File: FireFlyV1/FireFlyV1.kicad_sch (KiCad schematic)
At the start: 76 parts, among them J1 Conn_01x03, J2 Conn_01x03, J3 Conn_01x03, J4 Conn_01x03, J5 Conn_01x03, SW1 TS-1187A-B-A-B, SW2 TS-1187A-B-A-B, U1 RP2040, U2 W25Q32JVSS, U3 AMS1117-3.3, U5 MCP6001T-I/OT, U6 74HC595D,118, U7 PEC12R-4215F-S0024, X1 X322512MSB4SI

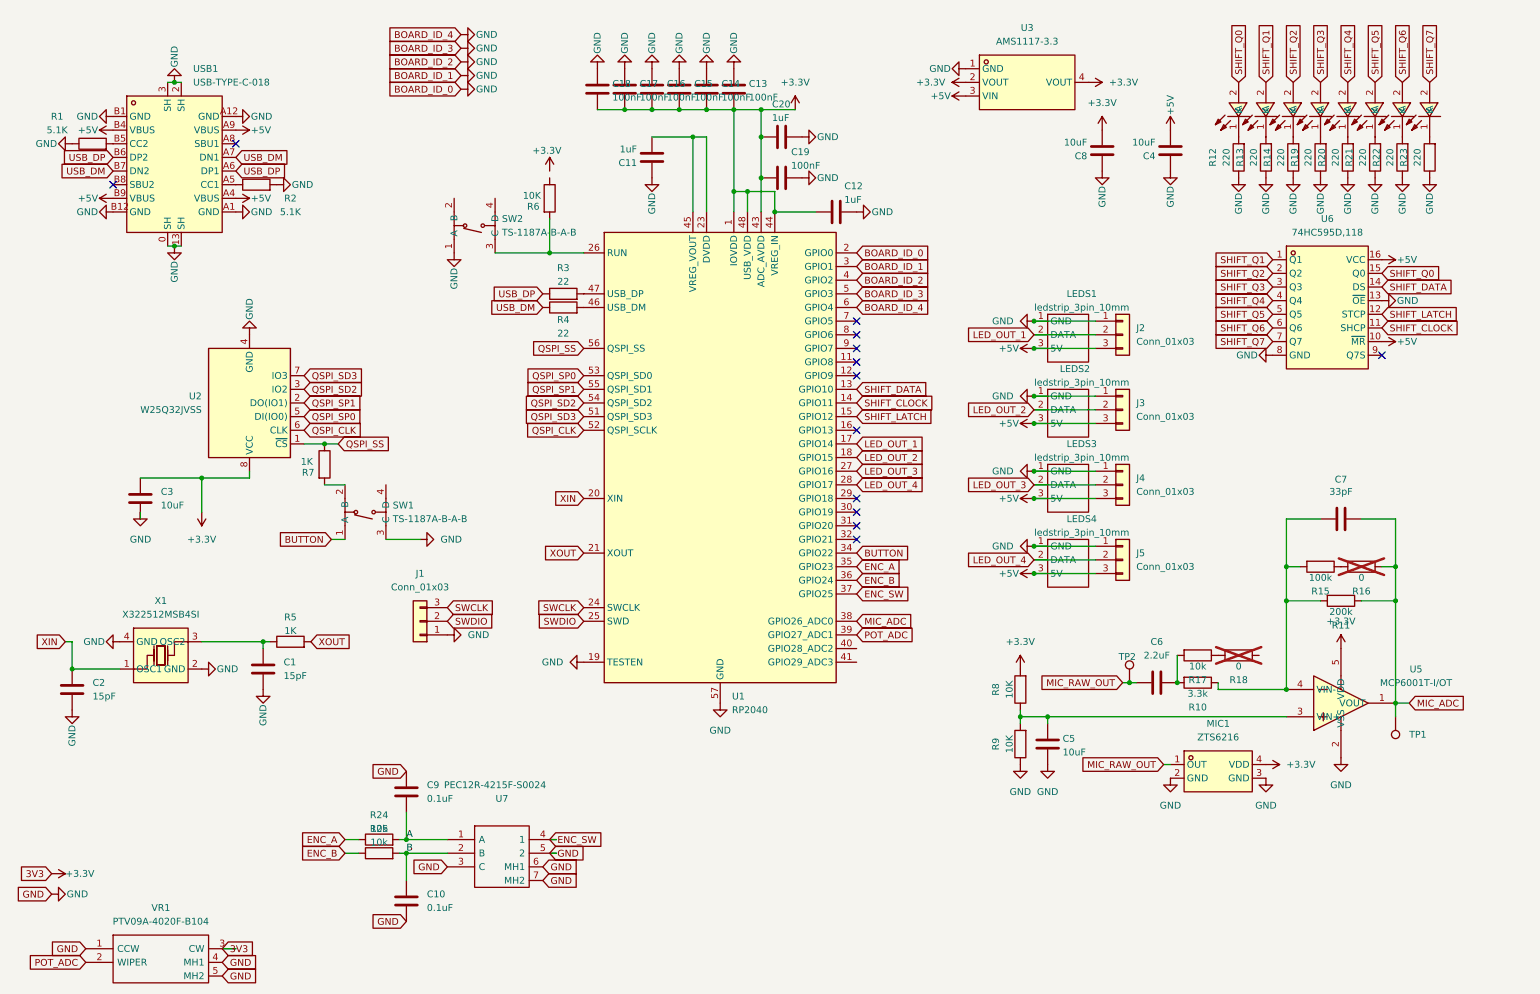
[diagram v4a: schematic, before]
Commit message: FireFlyV1 components layout initial thoughts
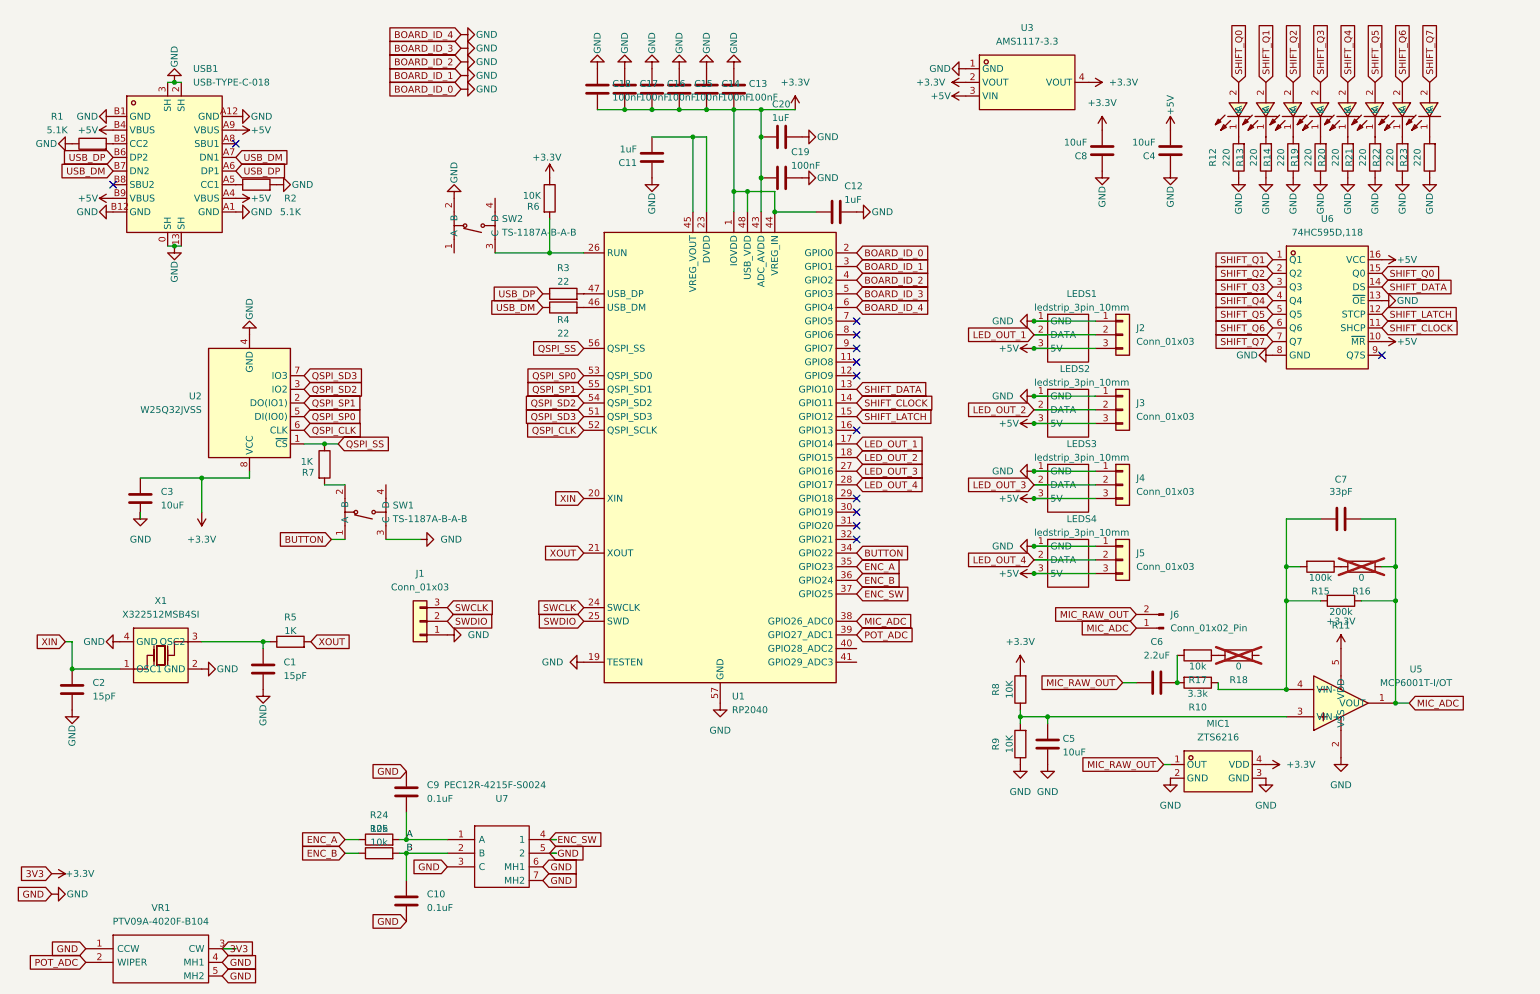
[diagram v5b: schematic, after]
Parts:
- removed TP1, TP2: TestPoint, TestPoint:TestPoint_Loop_D1.80mm_Drill1.0mm_Beaded, symbol Connector:TestPoint
- added J6: Conn_01x02_Pin, Connector_PinHeader_2.54mm:PinHeader_1x02_P2.54mm_Vertical, symbol Connector:Conn_01x02_Pin
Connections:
- net +3.3V: now also R6.1
- net GND: now also SW2.2 (B); no longer SW2.1 (A)
- net MIC_ADC: now also J6.1 (Pin_1)
- net MIC_RAW_OUT: now also J6.2 (Pin_2)

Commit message: FireFlyV1 mostly fit on the board
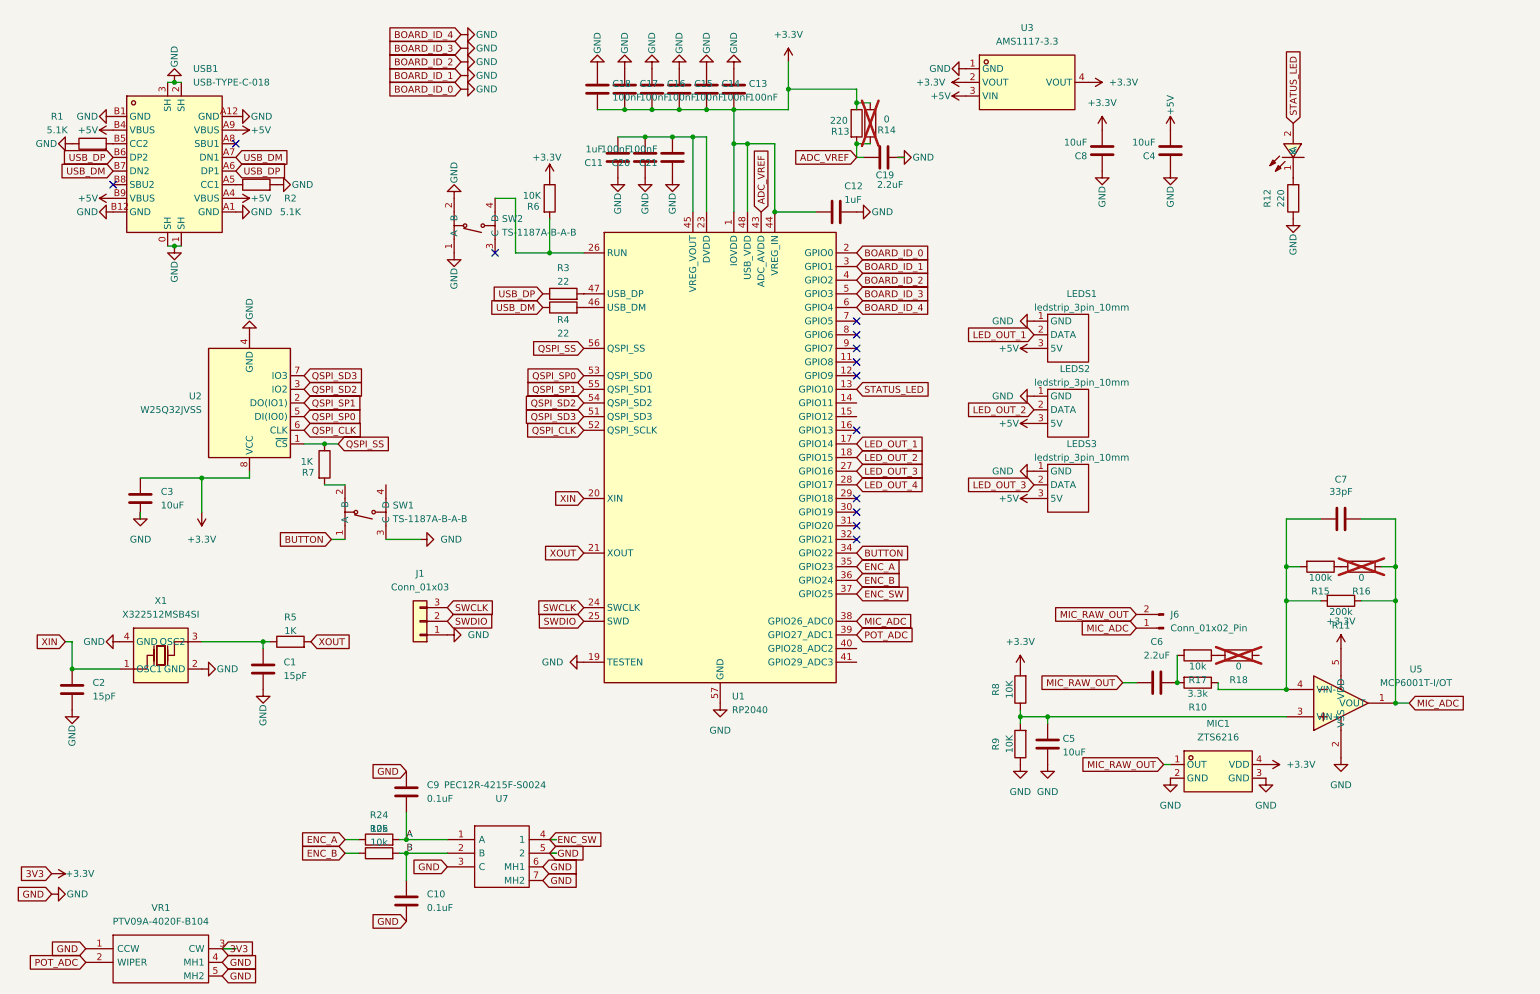
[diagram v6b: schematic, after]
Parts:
- removed J2, J3, J4, J5: Conn_01x03, Connector_PinHeader_2.54mm:PinHeader_1x03_P2.54mm_Vertical, symbol Connector_Generic:Conn_01x03
- removed LED2, LED3, LED4, LED5, LED6, LED7, LED8: KT-0603R, easyeda2kicad:LED0603-RD, symbol easyeda2kicad:KT-0603R
- removed LEDS4: ledstrip_3pin_10mm, mouser:ledstrip_3pin_10mm, symbol kylarLEDs:ledstrip_3pin_10mm
- removed R19, R20, R21, R22, R23: 220, Resistor_SMD:R_0402_1005Metric, symbol Device:R
- removed U6: 74HC595D,118, easyeda2kicad:SOIC-16_L9.9-W3.9-P1.27-LS6.0-BL, symbol easyeda2kicad:74HC595D,118
- added C21: 100nF, Capacitor_SMD:C_0402_1005Metric, symbol Device:C
- C19: value 100nF -> 2.2uF
- C20: value 1uF -> 100nF
- LEDS1, LEDS2, LEDS3: footprint mouser:ledstrip_3pin_10mm -> mouser:ledstrip_3pin_withpins
- R14: value 220 -> 0; now not fitted
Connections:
- net SHIFT_Q0 is gone; now on net STATUS_LED: LED1.2 (A)
- net +3.3V: now also R13.1, R14.1; no longer C19.1, C20.1, U1.43 (ADC_AVDD)
- net GND: now also SW2.1 (A), USB1.1 (SH), C21.2; no longer R13.1, R14.1, USB1.13 (SH)
- net ADC_VREF: now reaches R13.2
- net ADC_VREF: now also C19.1, R14.2, U1.43 (ADC_AVDD)
- net at C11.1, U1.23 (DVDD), U1.45 (VREG_VOUT)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: now also C20.1, C21.1
- net at R6.2, U1.26 (RUN): now also SW2.4 (D); no longer SW2.3 (C)
- net SHIFT_CLOCK: no longer names the net of U1.14 (GPIO11)
- net SHIFT_DATA renamed STATUS_LED
- net SHIFT_LATCH: no longer names the net of U1.15 (GPIO12)
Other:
- moved on the sheet: C11, C19, R12

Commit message: FireFlyV1 everything on board
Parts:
- removed J6: Conn_01x02_Pin, Connector_PinHeader_2.54mm:PinHeader_1x02_P2.54mm_Vertical, symbol Connector:Conn_01x02_Pin
- added J2, J3: Conn_01x01_Pin, Connector_PinHeader_2.54mm:PinHeader_1x01_P2.54mm_Vertical, symbol Connector:Conn_01x01_Pin
- C5: value 10uF -> 1uF
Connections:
- net MIC_ADC: now also J3.1 (Pin_1)
- net MIC_RAW_OUT: now also J2.1 (Pin_1)
- net at R18.1: now also C7.1, R10.1, R11.2, R15.2, U5.4 (VIN-)
- net LED_OUT_4: no longer names the net of U1.28 (GPIO17)
- no-connect marks 13 -> 14
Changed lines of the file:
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@@
 	)
 	(junction
+		(at 247.65 137.16)
+		(diameter 0)
+		(color 0 0 0 0)
+	)
+	(junction
 		(at 86.36 167.64)
 		(diameter 0)
@@
 	)
 	(no_connect
+		(at 170.18 99.06)
+	)
+	(no_connect
 		(at 31.75 43.18)
 	)
@@
 	(wire
 		(pts
+			(xy 247.65 137.16) (xy 237.49 137.16)
+		)
+		(stroke
+			(width 0)
+			(type default)
+		)
+	)
+	(wire
+		(pts
 			(xy 267.97 114.3) (xy 270.51 114.3)
 		)
@@
 	(wire
 		(pts
+			(xy 247.65 130.81) (xy 247.65 137.16)
+		)
+		(stroke
+			(width 0)
+			(type default)
+		)
+	)
+	(wire
+		(pts
 			(xy 250.19 120.65) (xy 256.54 120.65)
 		)
@@
 	(wire
 		(pts
-			(xy 250.19 137.16) (xy 237.49 137.16)
+			(xy 250.19 137.16) (xy 247.65 137.16)
 		)
 		(stroke
@@
 	(wire
 		(pts
+			(xy 245.11 130.81) (xy 247.65 130.81)
+		)
+		(stroke
+			(width 0)
+			(type default)
+		)
+	)
+	(wire
+		(pts
 			(xy 139.7 34.29) (xy 139.7 48.26)
 		)
@@
 		)
 	)
-	(global_label "LED_OUT_4"
-		(shape input)
-		(at 170.18 99.06 0)
-		(fields_autoplaced yes)
-		(effects
-			(font
-				(size 1.27 1.27)
-			)
-			(justify left)
-		)
-		(property "Intersheetrefs" "${INTERSHEET_REFS}"
-			(at 183.3856 99.06 0)
-			(effects
-				(font
-					(size 1.27 1.27)
-				)
-				(justify left)
-				(hide yes)
-			)
-		)
-	)
 	(global_label "MIC_RAW_OUT"
 		(shape input)
@@
 	)
 	(symbol
+		(lib_id "Connector:Conn_01x01_Pin")
+		(at 227.33 125.73 180)
+		(unit 1)
+		(exclude_from_sim no)
+		(in_bom yes)
+		(on_board yes)
+		(dnp no)
+		(fields_autoplaced yes)
+		(property "Reference" "J3"
+			(at 226.695 120.65 0)
+			(effects
+				(font
+					(size 1.27 1.27)
+				)
+			)
+		)
+		(property "Value" "Conn_01x01_Pin"
+			(at 226.695 123.19 0)
+			(effects
+				(font
+					(size 1.27 1.27)
+				)
+			)
+		)
+		(property "Footprint" "Connector_PinHeader_2.54mm:PinHeader_1x01_P2.54mm_Vertical"
+			(at 227.33 125.73 0)
+			(effects
+				(font
+					(size 1.27 1.27)
+				)
+				(hide yes)
+			)
+		)
+		(property "Datasheet" "~"
+			(at 227.33 125.73 0)
+			(effects
+				(font
+					(size 1.27 1.27)
+				)
+				(hide yes)
+			)
+		)
+		(property "Description" "Generic connector, single row, 01x01, script generated"
+			(at 227.33 125.73 0)
+			(effects
+				(font
+					(size 1.27 1.27)
+				)
+				(hide yes)
+			)
+		)
+		(pin "1"
+		)
+		(instances
+			(project "FireFlyV1"
+				(path "/72ac21c7-a543-4794-a410-99cf6f99d934"
+					(reference "J3")
+					(unit 1)
+				)
+			)
+		)
+	)
+	(symbol
 		(lib_id "MCU_RaspberryPi:RP2040")
 		(at 144.78 93.98 0)
@@
 	)
 	(symbol
+		(lib_id "Connector:Conn_01x01_Pin")
+		(at 227.33 123.19 180)
+		(unit 1)
+		(exclude_from_sim no)
+		(in_bom yes)
+		(on_board yes)
+		(dnp no)
+		(fields_autoplaced yes)
+		(property "Reference" "J2"
+			(at 226.695 118.11 0)
+			(effects
+				(font
+					(size 1.27 1.27)
+				)
+			)
+		)
+		(property "Value" "Conn_01x01_Pin"
+			(at 226.695 120.65 0)
+			(effects
+				(font
+					(size 1.27 1.27)
+				)
+			)
+		)
+		(property "Footprint" "Connector_PinHeader_2.54mm:PinHeader_1x01_P2.54mm_Vertical"
+			(at 227.33 123.19 0)
+			(effects
+				(font
+					(size 1.27 1.27)
+				)
+				(hide yes)
+			)
+		)
+		(property "Datasheet" "~"
+			(at 227.33 123.19 0)
+			(effects
+				(font
+					(size 1.27 1.27)
+				)
+				(hide yes)
+			)
+		)
+		(property "Description" "Generic connector, single row, 01x01, script generated"
+			(at 227.33 123.19 0)
+			(effects
+				(font
+					(size 1.27 1.27)
+				)
+				(hide yes)
+			)
+		)
+		(pin "1"
+		)
+		(instances
+			(project ""
+				(path "/72ac21c7-a543-4794-a410-99cf6f99d934"
+					(reference "J2")
+					(unit 1)
+				)
+			)
+		)
+	)
+	(symbol
 		(lib_name "ledstrip_3pin_10mm_1")
 		(lib_id "kylarLEDs:ledstrip_3pin_10mm")
@@
 			)
 		)
-		(property "Value" "10uF"
+		(property "Value" "1uF"
 			(at 208.534 148.844 0)
 			(effects
@@
 					(unit 1)
 				)
-			)
-		)
-	)
-	(symbol
-		(lib_id "Connector:Conn_01x02_Pin")
-		(at 227.33 125.73 180)
-		(unit 1)
-		(exclude_from_sim no)
-		(in_bom yes)
-		(on_board yes)
-		(dnp no)
-		(fields_autoplaced yes)
-		(property "Reference" "J6"
-			(at 228.6 123.1899 0)
-			(effects
-				(font
-					(size 1.27 1.27)
-				)
-				(justify right)
-			)
-		)
-		(property "Value" "Conn_01x02_Pin"
-			(at 228.6 125.7299 0)
-			(effects
-				(font
-					(size 1.27 1.27)
-				)
-				(justify right)
-			)
-		)
-		(property "Footprint" "Connector_PinHeader_2.54mm:PinHeader_1x02_P2.54mm_Vertical"
-			(at 227.33 125.73 0)
-			(effects
-				(font
-					(size 1.27 1.27)
-				)
-				(hide yes)
-			)
-		)
-		(property "Datasheet" "~"
-			(at 227.33 125.73 0)
-			(effects
-				(font
-					(size 1.27 1.27)
-				)
-				(hide yes)
-			)
-		)
-		(property "Description" "Generic connector, single row, 01x02, script generated"
-			(at 227.33 125.73 0)
-			(effects
-				(font
-					(size 1.27 1.27)
-				)
-				(hide yes)
-			)
-		)
-		(pin "2"
-		)
-		(pin "1"
-		)
-		(instances
-			(project ""
-				(path "/72ac21c7-a543-4794-a410-99cf6f99d934"
-					(reference "J6")
-					(unit 1)
-				)
